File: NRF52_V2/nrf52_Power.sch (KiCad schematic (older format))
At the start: 37 parts

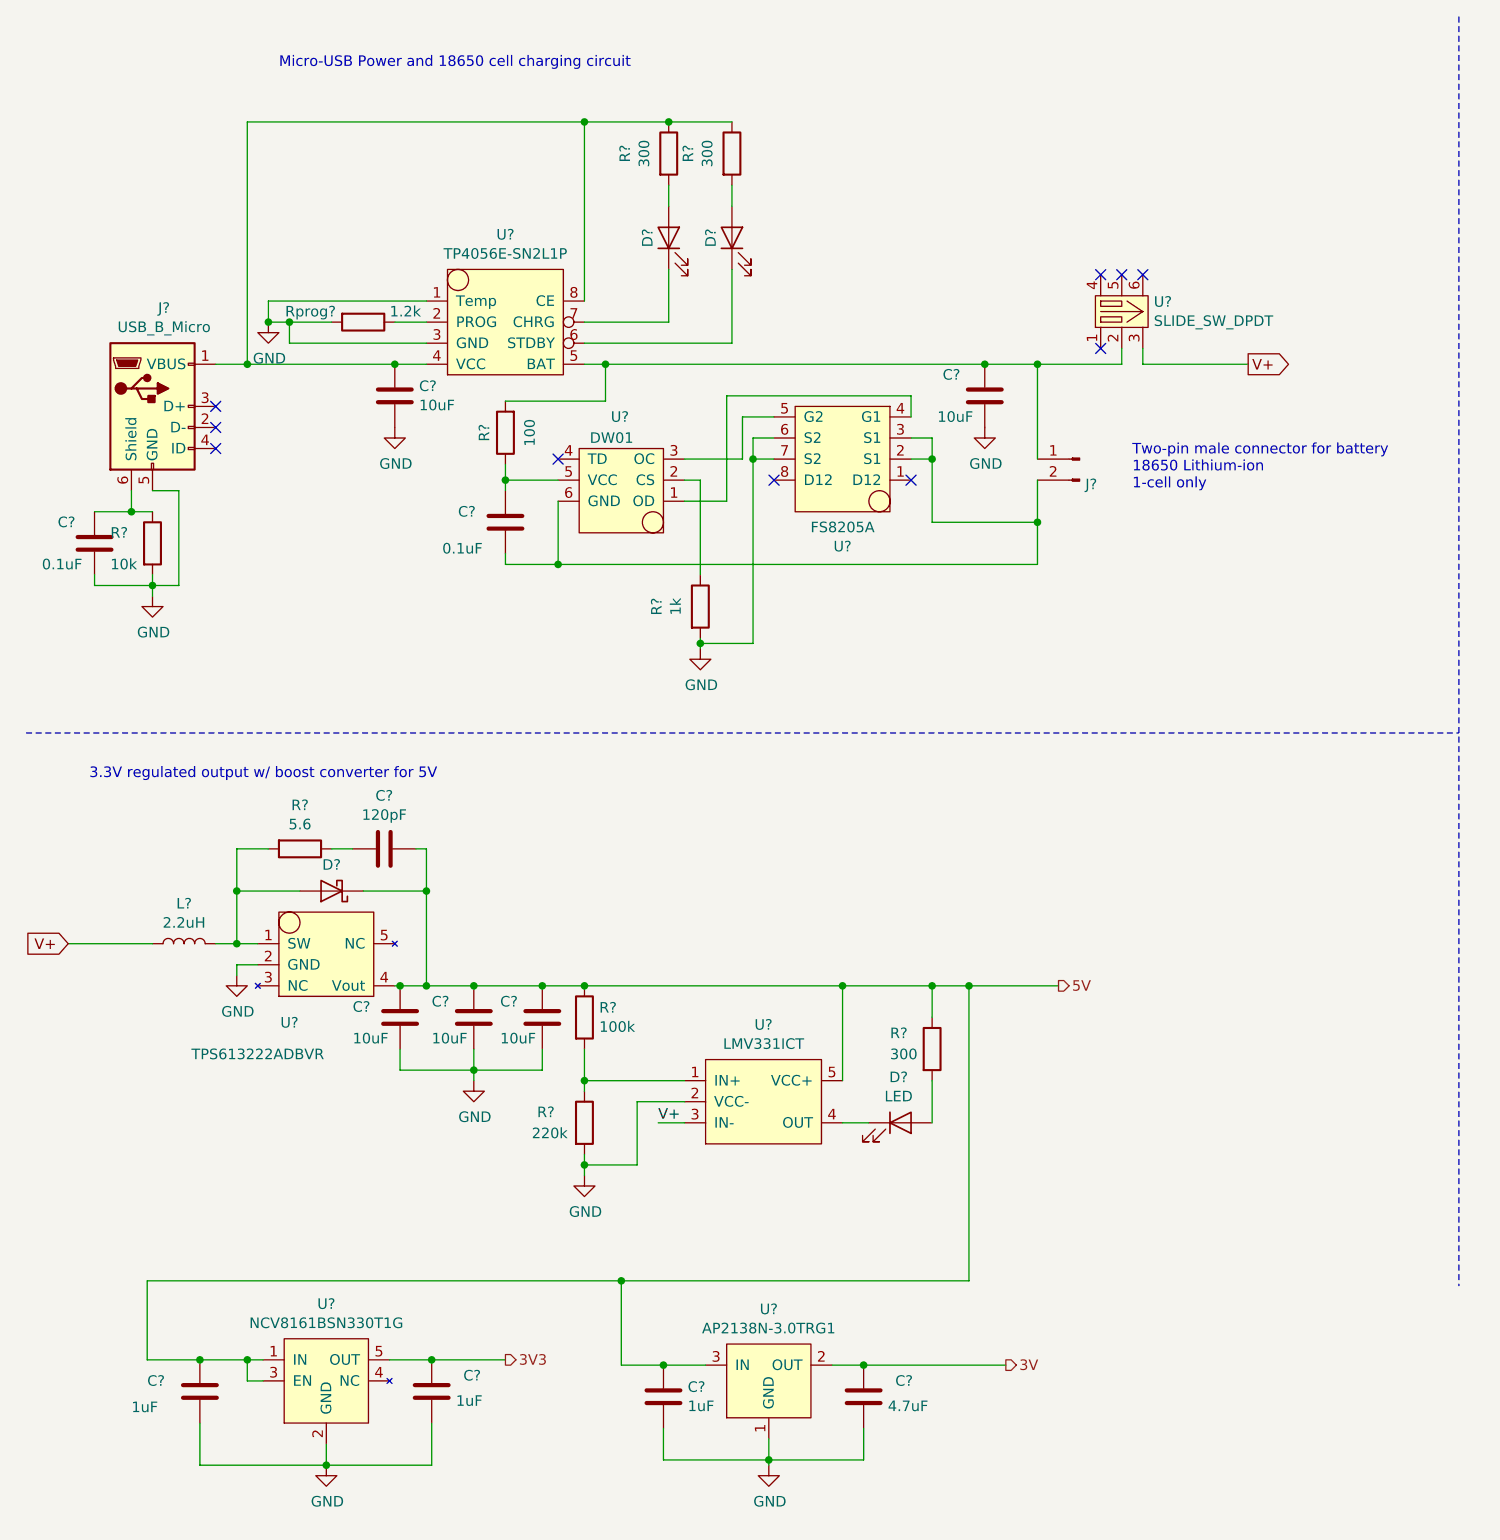
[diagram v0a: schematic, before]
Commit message: Added fuses to USB power and battery. Modified low battery LED circuit.
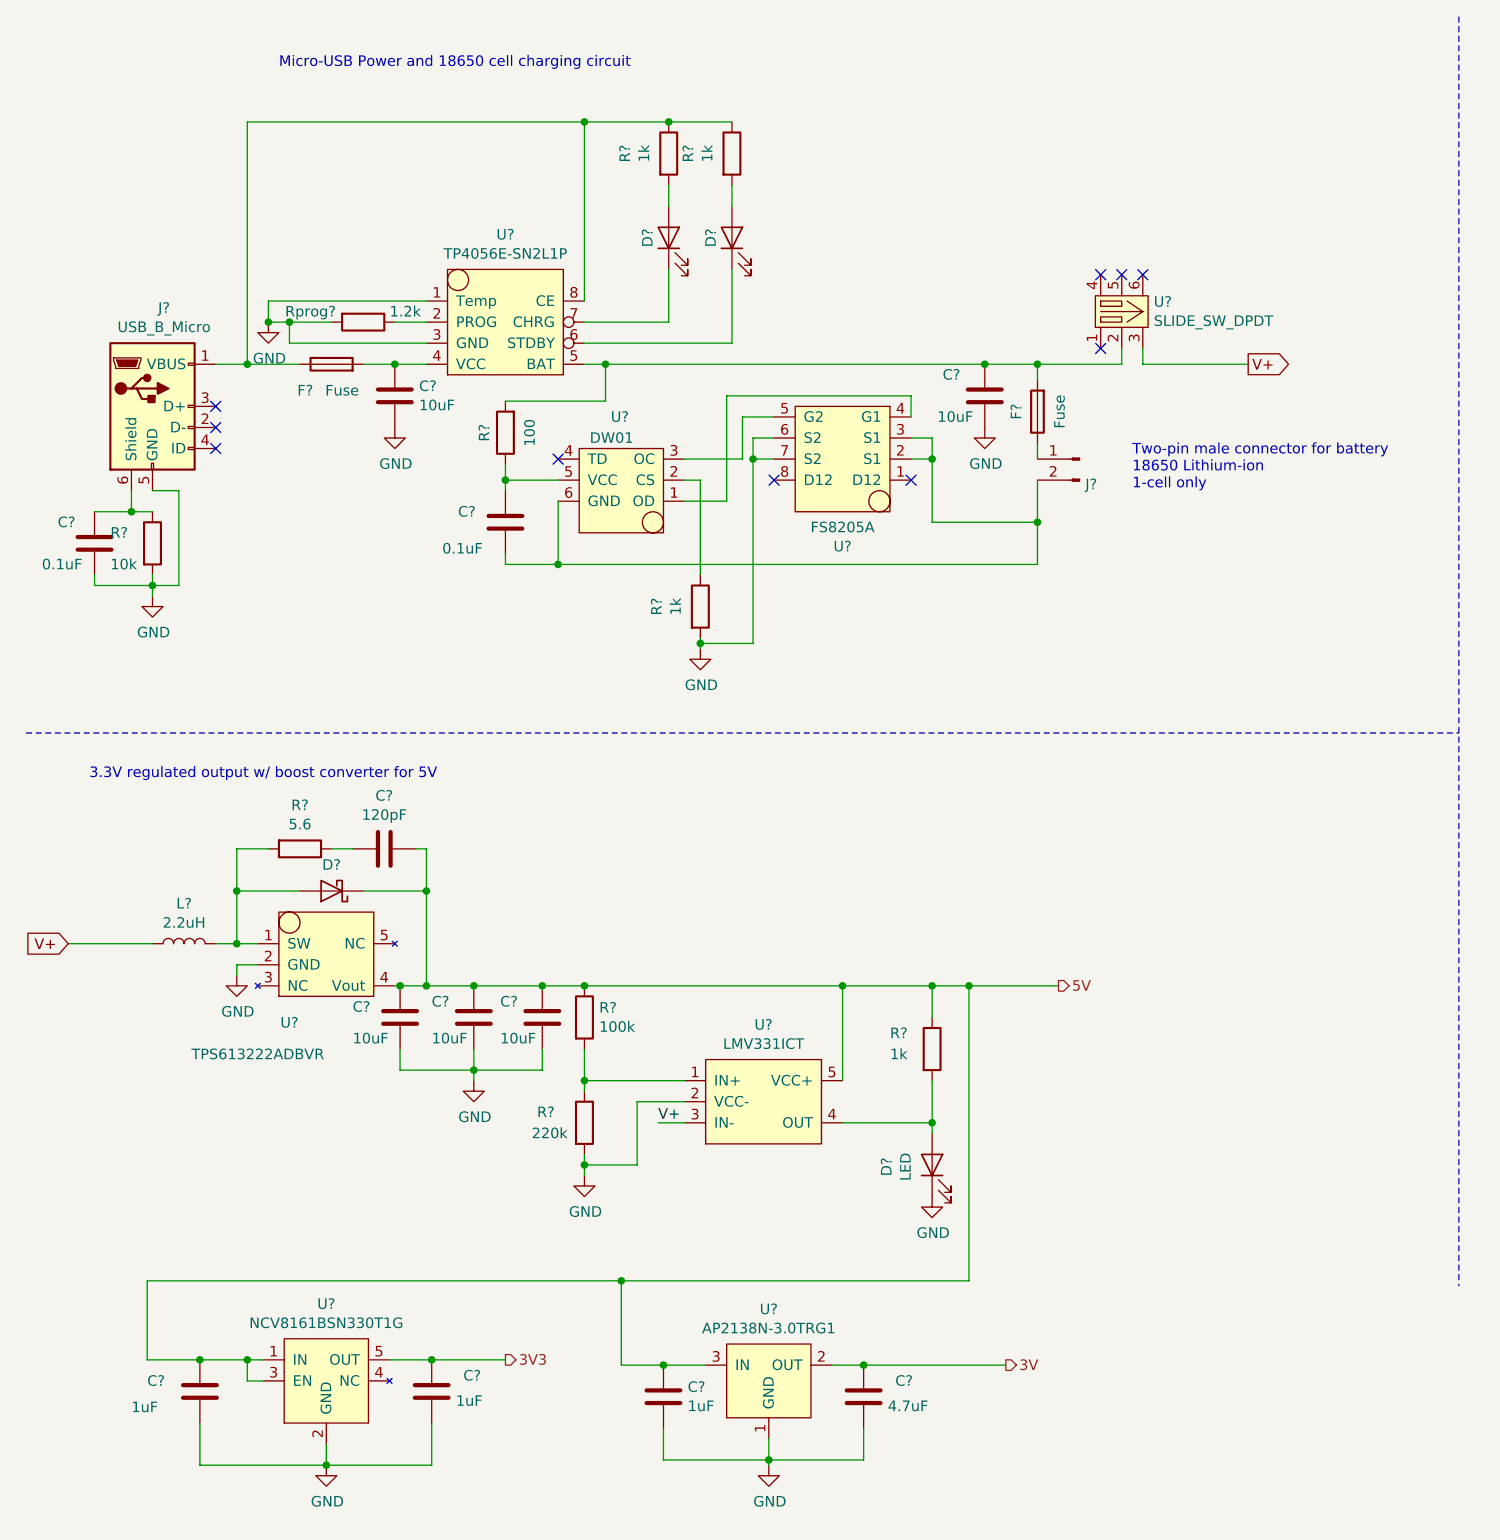
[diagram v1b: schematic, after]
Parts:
- added F? (x2): Fuse, symbol Device:Fuse
- R? (x3): value 300 -> 1k
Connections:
- net GND: now also D?.1 (K)
- net at J?.1 (VBUS), R?.1, R?.1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: now also F?.1; no longer C?.1, U?.4 (VCC)
- net at C?.1, R?.2, U?.2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: now also F?.2; no longer J?.1 (Pin_1)
- net at U?.4 (OUT): now also D?.2 (A), R?.2; no longer D?.1 (K)
- new net: F?.1, J?.1 (Pin_1)
- new net: C?.1, F?.2, U?.4 (VCC)
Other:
- moved on the sheet: D?
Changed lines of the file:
@@
 P 3850 1150
 F 0 "R?" V 3643 1150 50  0000 C CNN
-F 1 "300" V 3734 1150 50  0000 C CNN
+F 1 "1k" V 3734 1150 50  0000 C CNN
 F 2 "Resistor_SMD:R_0603_1608Metric_Pad1.05x0.95mm_HandSolder" V 3780 1150 50  0001 C CNN
 F 3 "~" H 3850 1150 50  0001 C CNN
@@
 P 3550 1150
 F 0 "R?" V 3343 1150 50  0000 C CNN
-F 1 "300" V 3434 1150 50  0000 C CNN
+F 1 "1k" V 3434 1150 50  0000 C CNN
 F 2 "Resistor_SMD:R_0603_1608Metric_Pad1.05x0.95mm_HandSolder" V 3480 1150 50  0001 C CNN
 F 3 "~" H 3550 1150 50  0001 C CNN
@@
 Wire Wire Line
 	1550 2150 1550 1000
-Connection ~ 1550 2150
-Wire Wire Line
-	1550 2150 2250 2150
 Connection ~ 3550 1000
 Wire Wire Line
@@
 	1    0    0    -1
 $EndComp
-Connection ~ 2250 2150
 Wire Wire Line
 	2250 2150 2400 2150
@@
 	1    0    0    -1
 $EndComp
-Wire Wire Line
-	5300 2600 5300 2150
 NoConn ~ 4050 2700
 NoConn ~ 4700 2700
-Connection ~ 5300 2150
 $Comp
 L Device:C C?
@@
 AR Path="/5BF5917C" Ref="C?"  Part="1"
 AR Path="/5BF31556/5BF5917C" Ref="C?"  Part="1"
+AR Path="/5C31A75C/5BF5917C" Ref="C?"  Part="1"
 F 0 "C?" H 1075 7075 50  0000 L CNN
 F 1 "1uF" H 1000 6950 50  0000 L CNN
@@
 AR Path="/5BF5918A" Ref="#PWR?"  Part="1"
 AR Path="/5BF31556/5BF5918A" Ref="#PWR?"  Part="1"
+AR Path="/5C31A75C/5BF5918A" Ref="#PWR?"  Part="1"
 F 0 "#PWR?" H 1925 7125 50  0001 C CNN
 F 1 "GND" H 1930 7202 50  0000 C CNN
@@
 AR Path="/5BF5919E" Ref="U?"  Part="1"
 AR Path="/5BF31556/5BF5919E" Ref="U?"  Part="1"
+AR Path="/5C31A75C/5BF5919E" Ref="U?"  Part="1"
 F 0 "U?" H 1750 4725 50  0000 C CNN
 F 1 "TPS613222ADBVR" H 1600 4575 50  0000 C CNN
@@
 AR Path="/5BF591A5" Ref="#PWR?"  Part="1"
 AR Path="/5BF31556/5BF591A5" Ref="#PWR?"  Part="1"
+AR Path="/5C31A75C/5BF591A5" Ref="#PWR?"  Part="1"
 F 0 "#PWR?" H 1500 4800 50  0001 C CNN
 F 1 "GND" H 1505 4877 50  0000 C CNN
@@
 AR Path="/5BF591B1" Ref="L?"  Part="1"
 AR Path="/5BF31556/5BF591B1" Ref="L?"  Part="1"
+AR Path="/5C31A75C/5BF591B1" Ref="L?"  Part="1"
 F 0 "L?" V 1440 4900 50  0000 C CNN
 F 1 "2.2uH" V 1349 4900 50  0000 C CNN
@@
 AR Path="/5BF591B8" Ref="C?"  Part="1"
 AR Path="/5BF31556/5BF591B8" Ref="C?"  Part="1"
+AR Path="/5C31A75C/5BF591B8" Ref="C?"  Part="1"
 F 0 "C?" H 2050 5300 50  0000 L CNN
 F 1 "10uF" H 2050 5150 50  0000 L CNN
@@
 AR Path="/5BF591BF" Ref="D?"  Part="1"
 AR Path="/5BF31556/5BF591BF" Ref="D?"  Part="1"
+AR Path="/5C31A75C/5BF591BF" Ref="D?"  Part="1"
 F 0 "D?" H 1950 4526 50  0000 C CNN
 F 1 "D_Schottky" H 1950 4525 50  0001 C CNN
@@
 AR Path="/5BF591C6" Ref="R?"  Part="1"
 AR Path="/5BF31556/5BF591C6" Ref="R?"  Part="1"
+AR Path="/5C31A75C/5BF591C6" Ref="R?"  Part="1"
 F 0 "R?" V 1593 4450 50  0000 C CNN
 F 1 "5.6" V 1684 4450 50  0000 C CNN
@@
 AR Path="/5BF591CD" Ref="C?"  Part="1"
 AR Path="/5BF31556/5BF591CD" Ref="C?"  Part="1"
+AR Path="/5C31A75C/5BF591CD" Ref="C?"  Part="1"
 F 0 "C?" V 1948 4450 50  0000 C CNN
 F 1 "120pF" V 2039 4450 50  0000 C CNN
@@
 AR Path="/5C0A07A3" Ref="#PWR?"  Part="1"
 AR Path="/5BF31556/5C0A07A3" Ref="#PWR?"  Part="1"
+AR Path="/5C31A75C/5C0A07A3" Ref="#PWR?"  Part="1"
 F 0 "#PWR?" H 3150 5750 50  0001 C CNN
 F 1 "GND" H 3155 5827 50  0000 C CNN
@@
 AR Path="/5BF59183" Ref="C?"  Part="1"
 AR Path="/5BF31556/5BF59183" Ref="C?"  Part="1"
+AR Path="/5C31A75C/5BF59183" Ref="C?"  Part="1"
 F 0 "C?" H 2575 7100 50  0000 L CNN
 F 1 "1uF" H 2540 6980 50  0000 L CNN
@@
 L Device:LED D?
 U 1 1 5C0C9C73
-P 4650 5750
-F 0 "D?" H 4641 5966 50  0000 C CNN
-F 1 "LED" H 4641 5875 50  0000 C CNN
-F 2 "LED_SMD:LED_0603_1608Metric_Pad1.05x0.95mm_HandSolder" H 4650 5750 50  0001 C CNN
-F 3 "~" H 4650 5750 50  0001 C CNN
-	1    4650 5750
-	1    0    0    -1
+P 4800 5950
+F 0 "D?" H 4791 6166 50  0000 C CNN
+F 1 "LED" H 4791 6075 50  0000 C CNN
+F 2 "LED_SMD:LED_0603_1608Metric_Pad1.05x0.95mm_HandSolder" H 4800 5950 50  0001 C CNN
+F 3 "~" H 4800 5950 50  0001 C CNN
+	1    4800 5950
+	0    -1   -1   0
 $EndComp
 $Comp
@@
 P 4800 5400
 F 0 "R?" H 4600 5475 50  0000 L CNN
-F 1 "300" H 4600 5375 50  0000 L CNN
+F 1 "1k" H 4600 5375 50  0000 L CNN
 F 2 "Resistor_SMD:R_0603_1608Metric_Pad1.05x0.95mm_HandSolder" V 4730 5400 50  0001 C CNN
 F 3 "~" H 4800 5400 50  0001 C CNN
@@
 	1    0    0    -1
 $EndComp
-Wire Wire Line
-	4500 5750 4375 5750
-Wire Wire Line
-	4800 5750 4800 5550
 Wire Wire Line
 	4800 5250 4800 5100
@@
 AR Path="/5C0FA0A1" Ref="C?"  Part="1"
 AR Path="/5BF31556/5C0FA0A1" Ref="C?"  Part="1"
+AR Path="/5C31A75C/5C0FA0A1" Ref="C?"  Part="1"
 F 0 "C?" H 2425 5325 50  0000 L CNN
 F 1 "10uF" H 2425 5150 50  0000 L CNN
@@
 AR Path="/5C0FA2D0" Ref="C?"  Part="1"
 AR Path="/5BF31556/5C0FA2D0" Ref="C?"  Part="1"
+AR Path="/5C31A75C/5C0FA2D0" Ref="C?"  Part="1"
 F 0 "C?" H 2750 5325 50  0000 L CNN
 F 1 "10uF" H 2750 5150 50  0000 L CNN
@@
 AR Path="/5C1005B2" Ref="#PWR?"  Part="1"
 AR Path="/5BF31556/5C1005B2" Ref="#PWR?"  Part="1"
+AR Path="/5C31A75C/5C1005B2" Ref="#PWR?"  Part="1"
 F 0 "#PWR?" H 2625 5300 50  0001 C CNN
 F 1 "GND" H 2630 5377 50  0000 C CNN
@@
 AR Path="/5C11B1D5" Ref="U?"  Part="1"
 AR Path="/5BF31556/5C11B1D5" Ref="U?"  Part="1"
+AR Path="/5C31A75C/5C11B1D5" Ref="U?"  Part="1"
 F 0 "U?" H 4025 7165 50  0000 C CNN
 F 1 "AP2138N-3.0TRG1" H 4025 7074 50  0000 C CNN
@@
 AR Path="/5C11B374" Ref="C?"  Part="1"
 AR Path="/5BF31556/5C11B374" Ref="C?"  Part="1"
+AR Path="/5C31A75C/5C11B374" Ref="C?"  Part="1"
 F 0 "C?" H 4625 7125 50  0000 L CNN
 F 1 "4.7uF" H 4590 7005 50  0000 L CNN
@@
 $EndComp
 Connection ~ 5050 2150
-Wire Wire Line
-	5050 2150 5300 2150
 Wire Wire Line
 	4050 2500 3950 2500
@@
 Wire Wire Line
 	5700 2150 5700 2075
-Wire Wire Line
-	5300 2150 5700 2150
 $Comp
 L Project_Libary:NCV8161BSN330T1G U?
@@
 Wire Wire Line
 	1550 6875 1625 6875
+$Comp
+L Device:Fuse F?
+U 1 1 5C31C1F3
+P 5300 2375
+F 0 "F?" V 5400 2375 50  0000 C CNN
+F 1 "Fuse" V 5194 2375 50  0000 C CNN
+F 2 "" V 5230 2375 50  0001 C CNN
+F 3 "~" H 5300 2375 50  0001 C CNN
+	1    5300 2375
+	-1   0    0    1
+$EndComp
+$Comp
+L power:GND #PWR?
+U 1 1 5C31FFF2
+P 4800 6100
+F 0 "#PWR?" H 4800 5850 50  0001 C CNN
+F 1 "GND" H 4805 5927 50  0000 C CNN
+F 2 "" H 4800 6100 50  0001 C CNN
+F 3 "" H 4800 6100 50  0001 C CNN
+	1    4800 6100
+	1    0    0    -1
+$EndComp
+Wire Wire Line
+	4800 5550 4800 5750
+Wire Wire Line
+	4375 5750 4800 5750
+Connection ~ 4800 5750
+Wire Wire Line
+	4800 5750 4800 5800
+Wire Wire Line
+	5050 2150 5300 2150
+Wire Wire Line
+	5300 2600 5300 2525
+Wire Wire Line
+	5300 2225 5300 2150
+Connection ~ 5300 2150
+Wire Wire Line
+	5300 2150 5700 2150
+$Comp
+L Device:Fuse F?
+U 1 1 5C338423
+P 1950 2150
+F 0 "F?" V 1825 2275 50  0000 C CNN
+F 1 "Fuse" V 1825 2100 50  0000 C CNN
+F 2 "" V 1880 2150 50  0001 C CNN
+F 3 "~" H 1950 2150 50  0001 C CNN
+	1    1950 2150
+	0    -1   -1   0
+$EndComp
+Wire Wire Line
+	2100 2150 2250 2150
+Connection ~ 2250 2150
+Wire Wire Line
+	1800 2150 1550 2150
+Connection ~ 1550 2150
 $EndSCHEMATC
